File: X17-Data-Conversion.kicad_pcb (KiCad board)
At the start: 2 copper layers, 41.5 x 37.3 mm, 30 parts, among them J1 Conn_01x05, J2 BG030_-_-_-_6_-_-_X_-_XXX_-_-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, J3 BG030_-_-_-_6_-_-_X_-_XXX_-_-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, SW1 1825910-6, U1 ABLS-8.000MHZ-B2-T, U2 STM32F091CCTx, U3 MAX485E

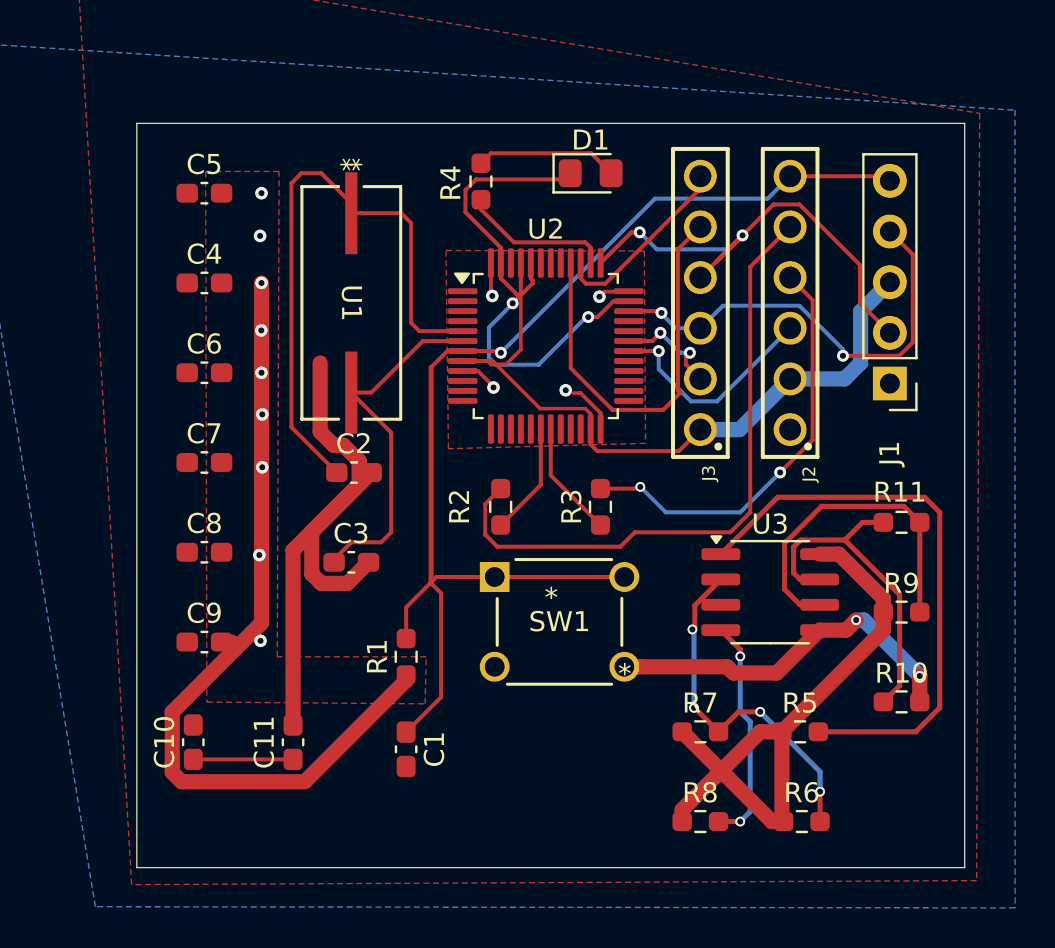
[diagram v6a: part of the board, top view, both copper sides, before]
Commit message: Redid to meet specifications no drcs
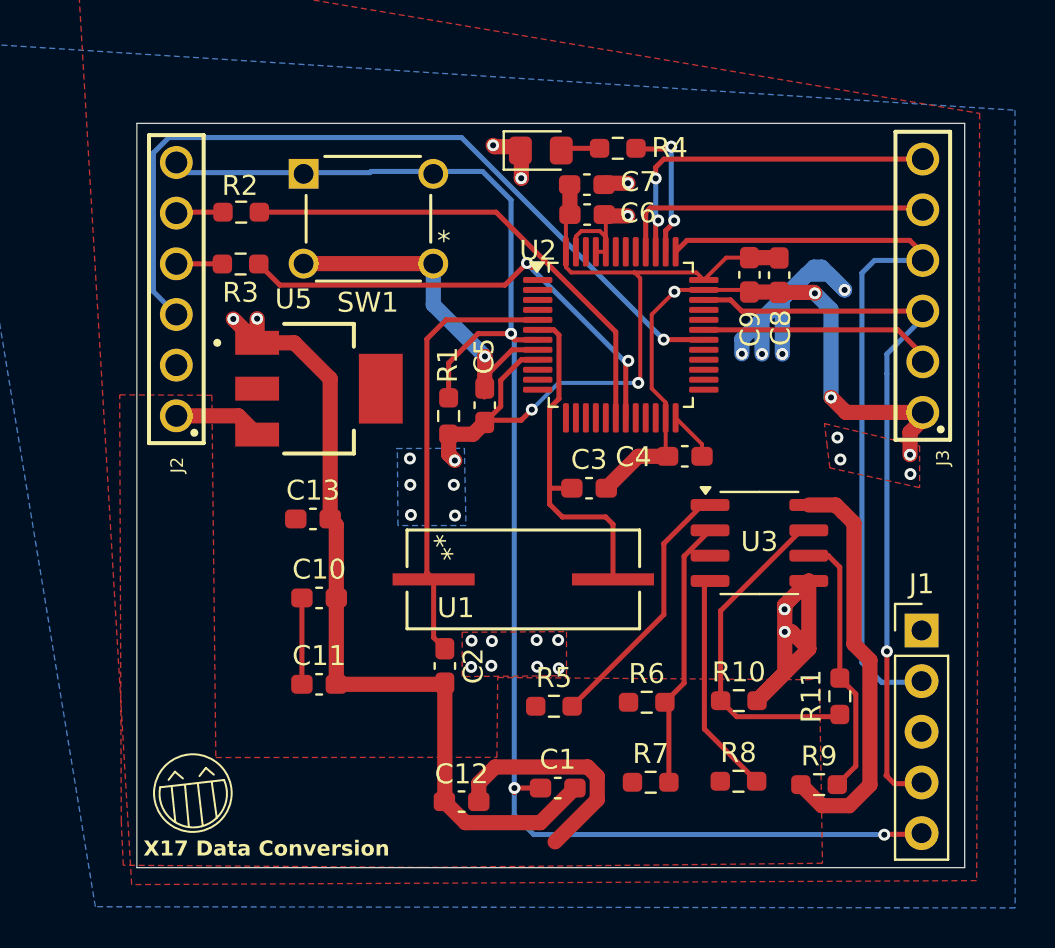
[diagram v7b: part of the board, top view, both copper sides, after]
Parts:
- added C12: 10uF, Capacitor_SMD:C_0603_1608Metric_Pad1.08x0.95mm_HandSolder, F.Cu at (157.0, 100.0)
- added C13: 22uF, Capacitor_SMD:C_0603_1608Metric_Pad1.08x0.95mm_HandSolder, F.Cu at (149.6, 85.8)
- added U5: AZ1117IH-3.3TRG1, AZ1117IH_3_3TRG1:SOT230P700X185-4N, F.Cu at (149.9, 79.3)
- moved C9 32.9 mm to (171.5, 73.6), turned to 90 degrees
- moved C8 32.0 mm to (172.9, 73.6), turned to 90 degrees
- moved J2 30.8 mm to (142.7, 74.3)
- moved C4 25.6 mm to (168.2, 82.7)
- moved C7 23.7 mm to (163.3, 69.1), turned to 180 degrees
- moved SW1 22.4 mm to (155.6, 73.0)
- moved R3 21.8 mm to (145.9, 73.0), turned to 180 degrees
- moved C6 20.8 mm to (163.3, 70.6), turned to 180 degrees
- moved R2 19.7 mm to (146.0, 70.5), turned to 180 degrees
- moved C5 17.6 mm to (158.2, 80.1), turned to -90 degrees
- moved U1 16.3 mm to (160.1, 88.9), turned to 0 degrees
- moved C3 12.5 mm to (163.4, 84.3)
- moved J1 12.5 mm to (180.1, 91.4), turned to 0 degrees
- moved R5 12.4 mm to (161.7, 95.2)
- moved R1 12.3 mm to (156.4, 80.7)
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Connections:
- J2 pad 1: 3.3V -> 5V
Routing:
- net C2_1: track 32.0 -> 2.36 mm
- net CLK: track 11.2 -> 40.7 mm
- net Net-(U2-PB0): track 5.66 -> 24.7 mm
- net C2_2: track 21.3 -> 2.31 mm, vias 2 -> 0
- net Net-(U2-PB1): track 5.84 -> 24.7 mm, vias 0 -> 2
- net NRST_PSB: track 59.5 -> 78.4 mm, vias 1 -> 3
- net USART1_RX: track 28.8 -> 13.2 mm
- net SWDIO: track 22.9 -> 38.2 mm, vias 2 -> 1
- net SWCLK: track 27.0 -> 40.5 mm, vias 2 -> 0
- net 3.3V: track 48.5 -> 61.1 mm, vias 13 -> 12
- net ALERT2: track 9.48 -> 18.4 mm, vias 0 -> 2
- net /OSC_IN: track 30.7 -> 21.9 mm
- net GND: track 113.0 -> 120.5 mm, vias 4 -> 24
- net DATA: track 5.46 -> 12.0 mm, vias 2 -> 0
- net Net-(D1-A): track 7.15 -> 1.91 mm
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- added copper zone on F.Cu, net 5V
- added copper zone on B.Cu, net GND

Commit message: meeting today, need to rewire
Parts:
- removed J2, J3: BG030_-_-_-_6_-_-_X_-_XXX_-_-_REVG5, 61300611121:61300611121
- removed U1: ABLS-8.000MHZ-B2-T, footprints2:ABLS-8.000MHZ-B2-T_ABR
- added C1: 0.1uF, Capacitor_SMD:C_0603_1608Metric_Pad1.08x0.95mm_HandSolder, F.Cu at (125.5, 74.9)
- added D2: LED, LED_SMD:LED_0805_2012Metric_Pad1.15x1.40mm_HandSolder, F.Cu at (127.2, 89.4)
- added J4: Conn_01x12_Pin, Library:Data Conversion two 1x6, F.Cu at (130.8, 50.1)
- added R2: 470, Resistor_SMD:R_0603_1608Metric_Pad0.98x0.95mm_HandSolder, F.Cu at (126.9, 92.2)
- added U4: MAX7375AXR805+T, footprints4:21-0075D_MXM, F.Cu at (112.4, 72.9)
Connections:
- C10 pad 1: Net-(C10-Pad1) -> 5V
- C11 pad 1: Net-(C10-Pad1) -> 5V
- U2 pad 13: unconnected-(U2-PA3-Pad13) -> PG
- U2 pad 14: ADC_IN1 -> unconnected-(U2-PA4-Pad14)
- U2 pad 15: ADC_IN0 -> unconnected-(U2-PA5-Pad15)
- U2 pad 16: ADC_IN2 -> unconnected-(U2-PA6-Pad16)
- U2 pad 18: Net-(U2-PB0) -> unconnected-(U2-PB0-Pad18)
- U2 pad 19: Net-(U2-PB1) -> unconnected-(U2-PB1-Pad19)
- U2 pad 30: CLK -> I2C1_SCL
- U2 pad 31: DATA -> I2C1_SDA
- U2 pad 33: unconnected-(U2-PA12-Pad33) -> USART1_DE
- U2 pad 39: ALERT2 -> unconnected-(U2-PB3-Pad39)
- U2 pad 41: unconnected-(U2-PB5-Pad41) -> I2C1_SMBA
- U2 pad 42: unconnected-(U2-PB6-Pad42) -> USART1_TX
- U2 pad 43: unconnected-(U2-PB7-Pad43) -> USART1_RX
- U2 pad 5: /OSC_IN -> Net-(U2-PF0)
- U2 pad 6: /OSC_OUT -> unconnected-(U2-PF1-Pad6)
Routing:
- net I2C1_SCL: track 0.00 -> 40.7 mm, vias 0 -> 1
- net CLK: track 40.7 -> 0.00 mm, vias 1 -> 0
- net unconnected-(U2-PB3-Pad39): track 0.00 -> 18.4 mm, vias 0 -> 2
- net ALERT2: track 18.4 -> 0.00 mm, vias 2 -> 0
- net 5V: track 36.4 -> 49.9 mm
- net I2C1_SDA: track 0.00 -> 12.0 mm
- net DATA: track 12.0 -> 0.00 mm
- net (no net): track 0.00 -> 6.85 mm
- net Net-(C10-Pad1): track 4.33 -> 0.00 mm
